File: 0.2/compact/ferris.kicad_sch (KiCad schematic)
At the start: 102 parts, among them J1 TYPE-C-31-M-12, K0_0 KEYSW, K0_1 KEYSW, K0_2 KEYSW, K0_3 KEYSW, K0_4 KEYSW, K0_5 KEYSW, K0_6 KEYSW, K0_7 KEYSW, K0_8 KEYSW, K0_9 KEYSW, K1_0 KEYSW, K1_1 KEYSW, K1_2 KEYSW, K1_3 KEYSW, K1_4 KEYSW, K1_5 KEYSW, K1_6 KEYSW, K1_7 KEYSW, K1_8 KEYSW, K1_9 KEYSW, K2_0 KEYSW, K2_1 KEYSW, K2_2 KEYSW, K2_3 KEYSW, K2_4 KEYSW, K2_5 KEYSW, K2_6 KEYSW, K2_7 KEYSW, K2_8 KEYSW, K2_9 KEYSW, K3_3 KEYSW, K3_4 KEYSW, K3_5 KEYSW, K3_6 KEYSW, Q1 PDTC123JT,215, SW1 B3U-1000P, U1 STM32F072CBT6, U2 MCP23017-E/SO, U3 MCP1700T-3302E/TT, U4 SRV05-4

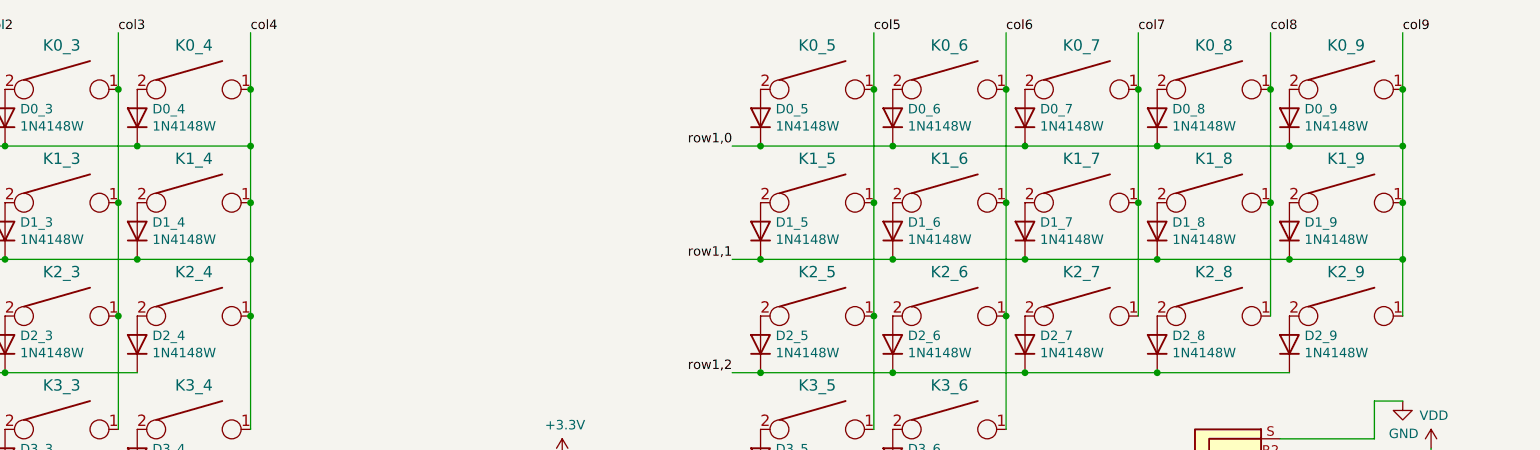
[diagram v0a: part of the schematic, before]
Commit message: Again, fix schematic bug connecting rows directly to rightmost column
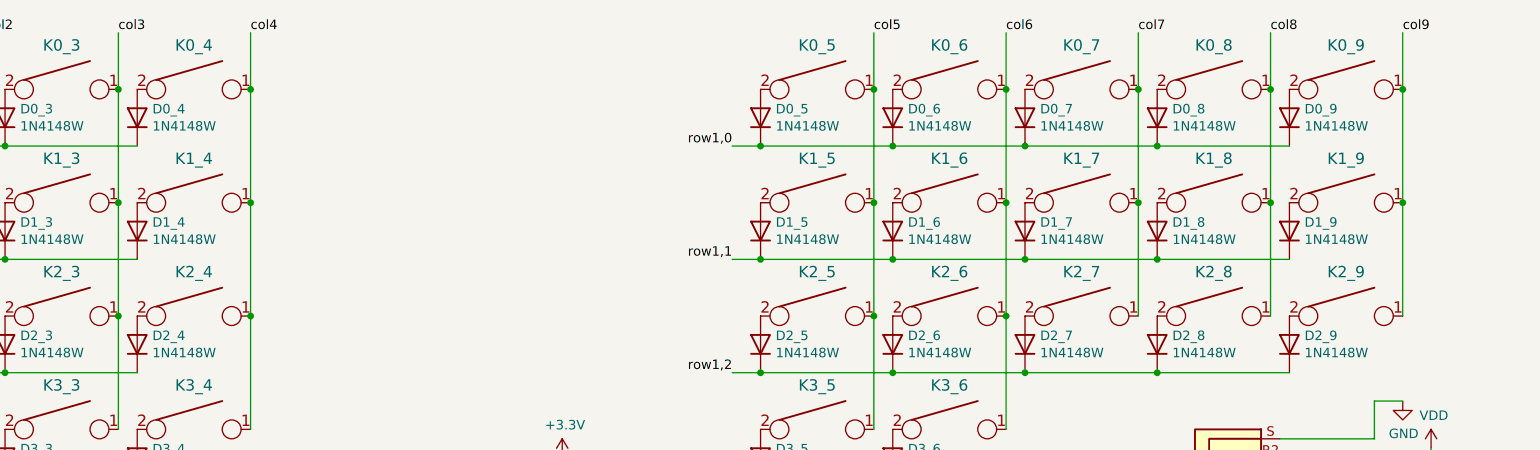
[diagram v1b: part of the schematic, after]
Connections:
- net col4: no longer D0_0.1 (K), D0_1.1 (K), D0_2.1 (K), D0_3.1 (K), D0_4.1 (K), D1_0.1 (K), D1_1.1 (K), D1_2.1 (K), D1_3.1 (K), D1_4.1 (K), U1.42 (PB6), U1.43 (PB7)
- net col9: no longer D0_5.1 (K), D0_6.1 (K), D0_7.1 (K), D0_8.1 (K), D0_9.1 (K), D1_5.1 (K), D1_6.1 (K), D1_7.1 (K), D1_8.1 (K), D1_9.1 (K), U2.1 (GPB0), U2.2 (GPB1)
- new net row0,0: D0_0.1 (K), D0_1.1 (K), D0_2.1 (K), D0_3.1 (K), D0_4.1 (K), U1.43 (PB7)
- new net row0,1: D1_0.1 (K), D1_1.1 (K), D1_2.1 (K), D1_3.1 (K), D1_4.1 (K), U1.42 (PB6)
- new net row1,0: D0_5.1 (K), D0_6.1 (K), D0_7.1 (K), D0_8.1 (K), D0_9.1 (K), U2.1 (GPB0)
- new net row1,1: D1_5.1 (K), D1_6.1 (K), D1_7.1 (K), D1_8.1 (K), D1_9.1 (K), U2.2 (GPB1)
